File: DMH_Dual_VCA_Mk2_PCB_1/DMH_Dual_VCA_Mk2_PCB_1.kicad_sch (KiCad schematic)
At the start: 0 parts

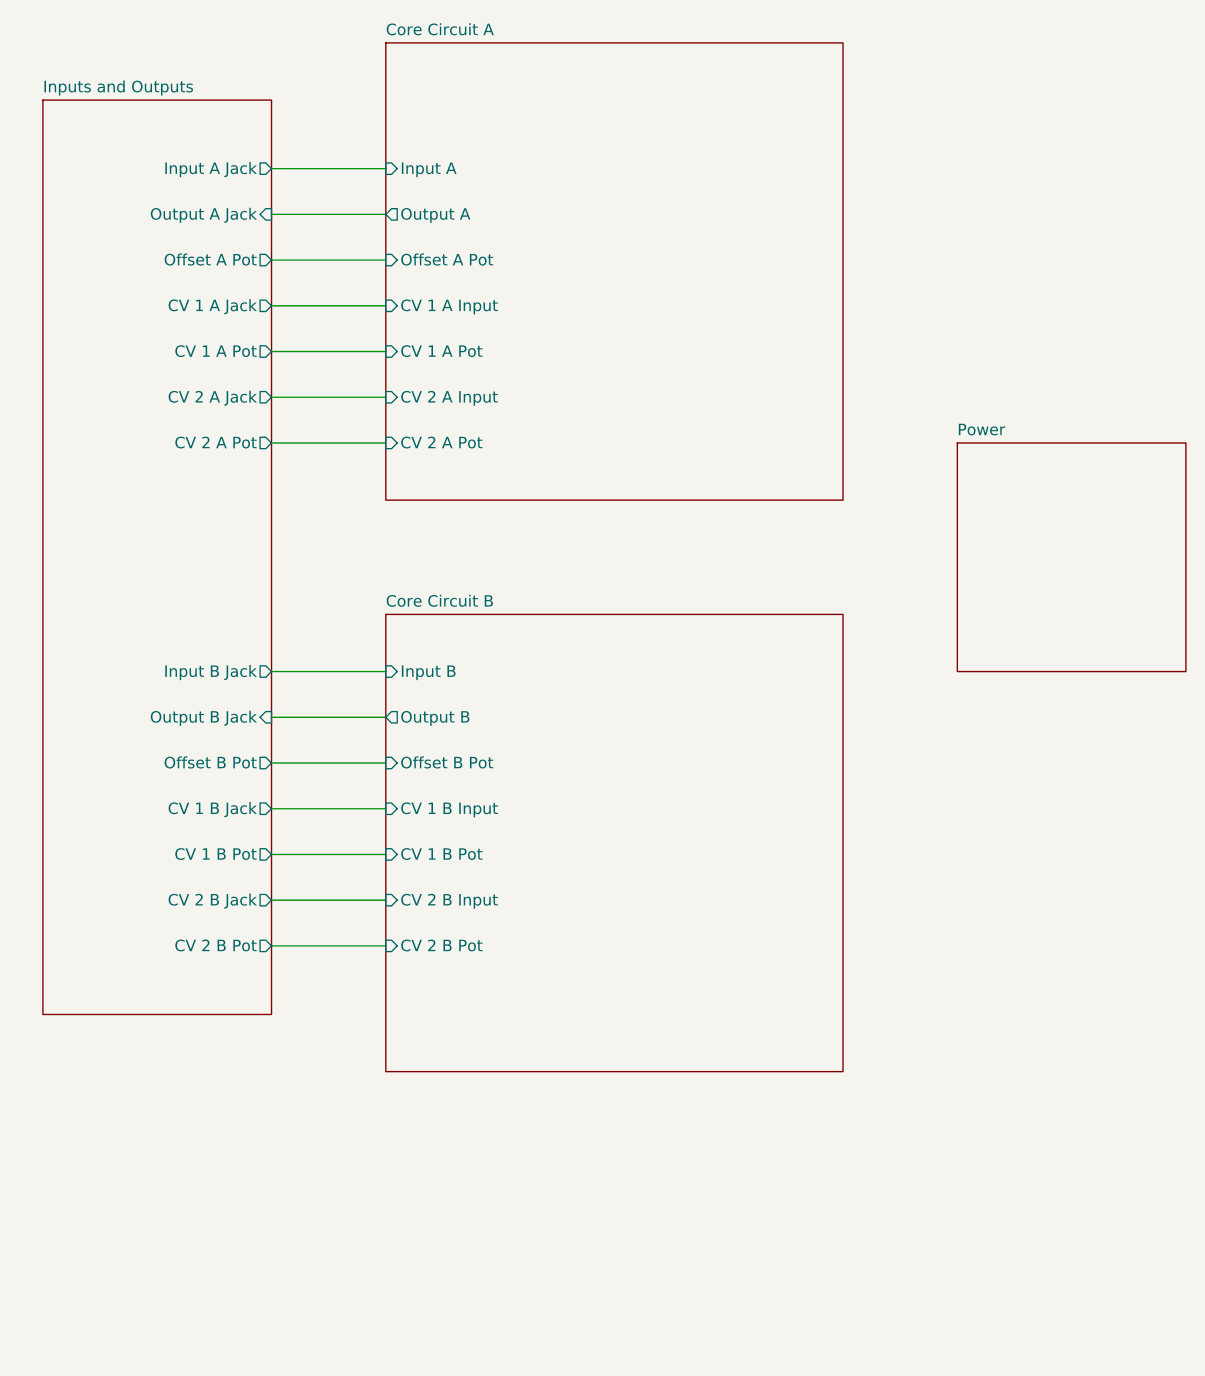
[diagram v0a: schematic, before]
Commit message: Finished schematic for PCB 1
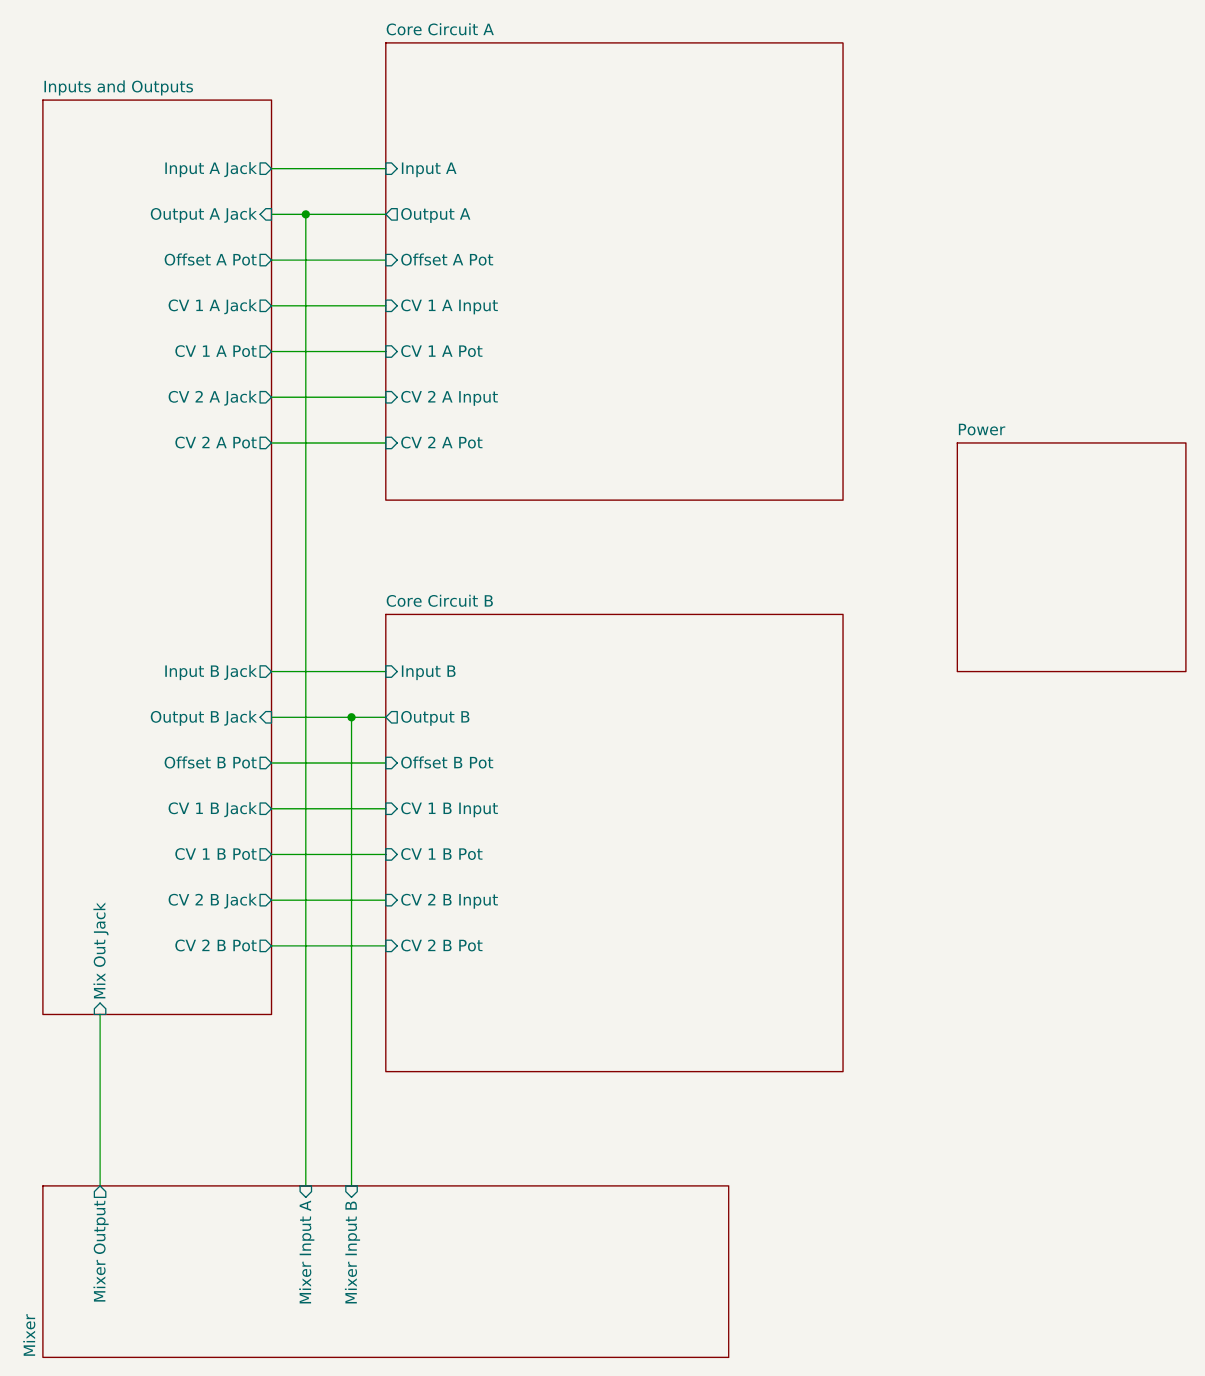
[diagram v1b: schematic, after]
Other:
- added sheet Mixer (Mixer.kicad_sch)
- sheet Inputs and Outputs ports: added Mix Out Jack; removed none
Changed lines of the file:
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@@
 		(comment 1 "PCB for 5 cm Kosmo format synthesizer module")
 	)
+	(junction
+		(at 54.61 63.5)
+		(diameter 0)
+		(color 0 0 0 0)
+	)
+	(junction
+		(at 59.69 119.38)
+		(diameter 0)
+		(color 0 0 0 0)
+	)
 	(wire
 		(pts
@@
 	(wire
 		(pts
-			(xy 50.8 63.5) (xy 63.5 63.5)
+			(xy 31.75 152.4) (xy 31.75 171.45)
+		)
+		(stroke
+			(width 0)
+			(type default)
+		)
+	)
+	(wire
+		(pts
+			(xy 50.8 63.5) (xy 54.61 63.5)
 		)
 		(stroke
@@
 	(wire
 		(pts
+			(xy 59.69 119.38) (xy 59.69 171.45)
+		)
+		(stroke
+			(width 0)
+			(type default)
+		)
+	)
+	(wire
+		(pts
+			(xy 59.69 119.38) (xy 63.5 119.38)
+		)
+		(stroke
+			(width 0)
+			(type default)
+		)
+	)
+	(wire
+		(pts
+			(xy 54.61 63.5) (xy 63.5 63.5)
+		)
+		(stroke
+			(width 0)
+			(type default)
+		)
+	)
+	(wire
+		(pts
 			(xy 50.8 78.74) (xy 63.5 78.74)
 		)
@@
 	(wire
 		(pts
-			(xy 50.8 119.38) (xy 63.5 119.38)
+			(xy 54.61 63.5) (xy 54.61 171.45)
+		)
+		(stroke
+			(width 0)
+			(type default)
+		)
+	)
+	(wire
+		(pts
+			(xy 50.8 119.38) (xy 59.69 119.38)
 		)
 		(stroke
@@
 		)
 		(instances
-			(project "DMH_Transistor_VCA_PCB"
+			(project "DMH_Dual_VCA_Mk2_PCB_1"
 				(path "/58f4306d-5387-4983-bb08-41a2313fd315"
 					(page "4")
+				)
+			)
+		)
+	)
+	(sheet
+		(at 25.4 171.45)
+		(size 76.2 19.05)
+		(exclude_from_sim no)
+		(in_bom yes)
+		(on_board yes)
+		(dnp no)
+		(fields_autoplaced yes)
+		(stroke
+			(width 0.1524)
+			(type solid)
+		)
+		(fill
+			(color 0 0 0 0.0000)
+		)
+		(property "Sheetname" "Mixer"
+			(at 24.6884 190.5 90)
+			(effects
+				(font
+					(size 1.27 1.27)
+				)
+				(justify left bottom)
+			)
+		)
+		(property "Sheetfile" "Mixer.kicad_sch"
+			(at 102.1846 190.5 90)
+			(effects
+				(font
+					(size 1.27 1.27)
+				)
+				(justify left top)
+				(hide yes)
+			)
+		)
+		(pin "Mixer Input A" input
+			(at 54.61 171.45 90)
+			(effects
+				(font
+					(size 1.27 1.27)
+				)
+				(justify right)
+			)
+		)
+		(pin "Mixer Input B" input
+			(at 59.69 171.45 90)
+			(effects
+				(font
+					(size 1.27 1.27)
+				)
+				(justify right)
+			)
+		)
+		(pin "Mixer Output" output
+			(at 31.75 171.45 90)
+			(effects
+				(font
+					(size 1.27 1.27)
+				)
+				(justify right)
+			)
+		)
+		(instances
+			(project "DMH_Dual_VCA_Mk2_PCB_1"
+				(path "/58f4306d-5387-4983-bb08-41a2313fd315"
+					(page "6")
 				)
 			)
@@
 		)
 		(instances
-			(project "DMH_Transistor_VCA_PCB"
+			(project "DMH_Dual_VCA_Mk2_PCB_1"
 				(path "/58f4306d-5387-4983-bb08-41a2313fd315"
 					(page "5")
@@
 		)
 		(instances
-			(project "DMH_Transistor_VCA_PCB"
+			(project "DMH_Dual_VCA_Mk2_PCB_1"
 				(path "/58f4306d-5387-4983-bb08-41a2313fd315"
 					(page "3")
@@
 			)
 		)
+		(pin "Mix Out Jack" input
+			(at 31.75 152.4 270)
+			(effects
+				(font
+					(size 1.27 1.27)
+				)
+				(justify left)
+			)
+		)
 		(instances
-			(project "DMH_Transistor_VCA_PCB"
+			(project "DMH_Dual_VCA_Mk2_PCB_1"
 				(path "/58f4306d-5387-4983-bb08-41a2313fd315"
 					(page "2")
